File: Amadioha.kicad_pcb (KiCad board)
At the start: 4 copper layers, 74 x 49.9 mm, 66 parts, among them IC1 ACS37800KMACTR-030B3-I2C, J1 691137710002, J2 SW_Debug, J3 691137710002, K1 G6DN-1A-SL_DC5, Q1 BSS138, Q2 BSS138, Q3 BSS138, SW1 PTS815, SW2 PTS815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

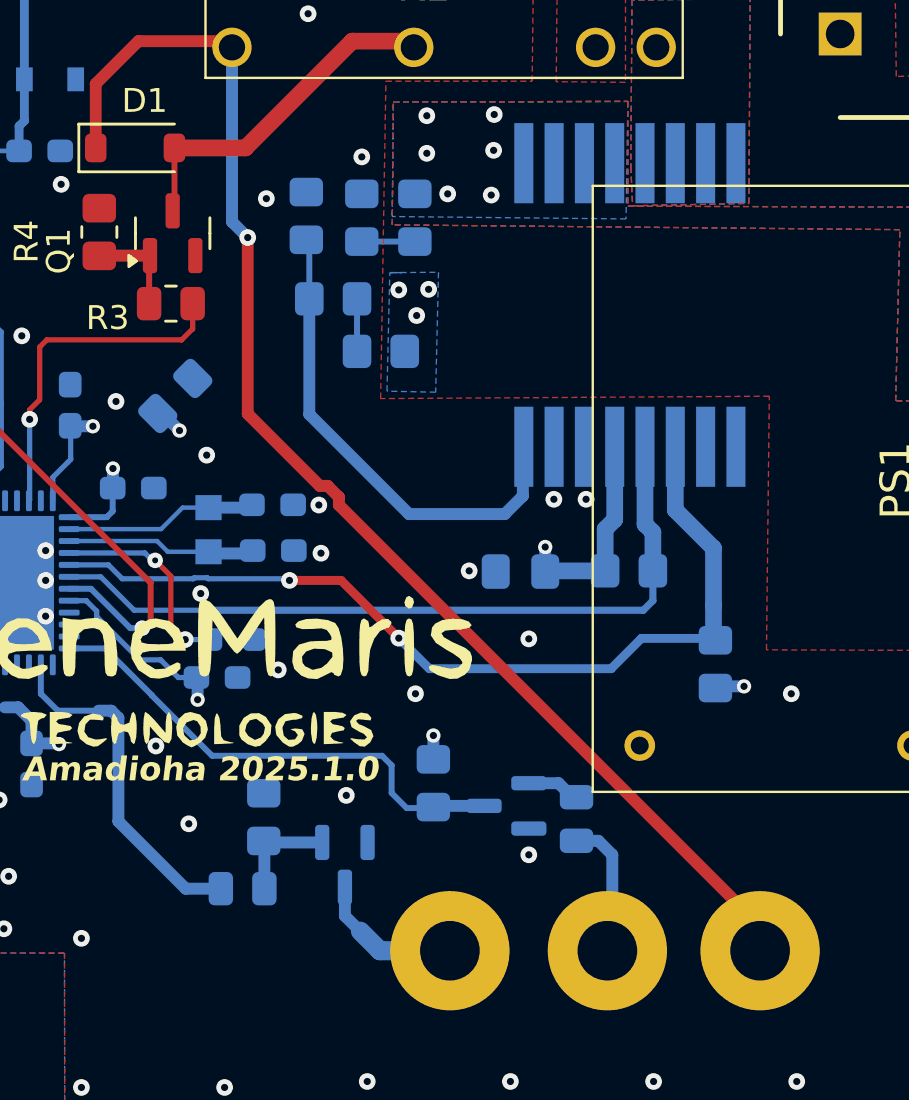
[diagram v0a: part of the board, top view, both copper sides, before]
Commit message: trace width ajdustment
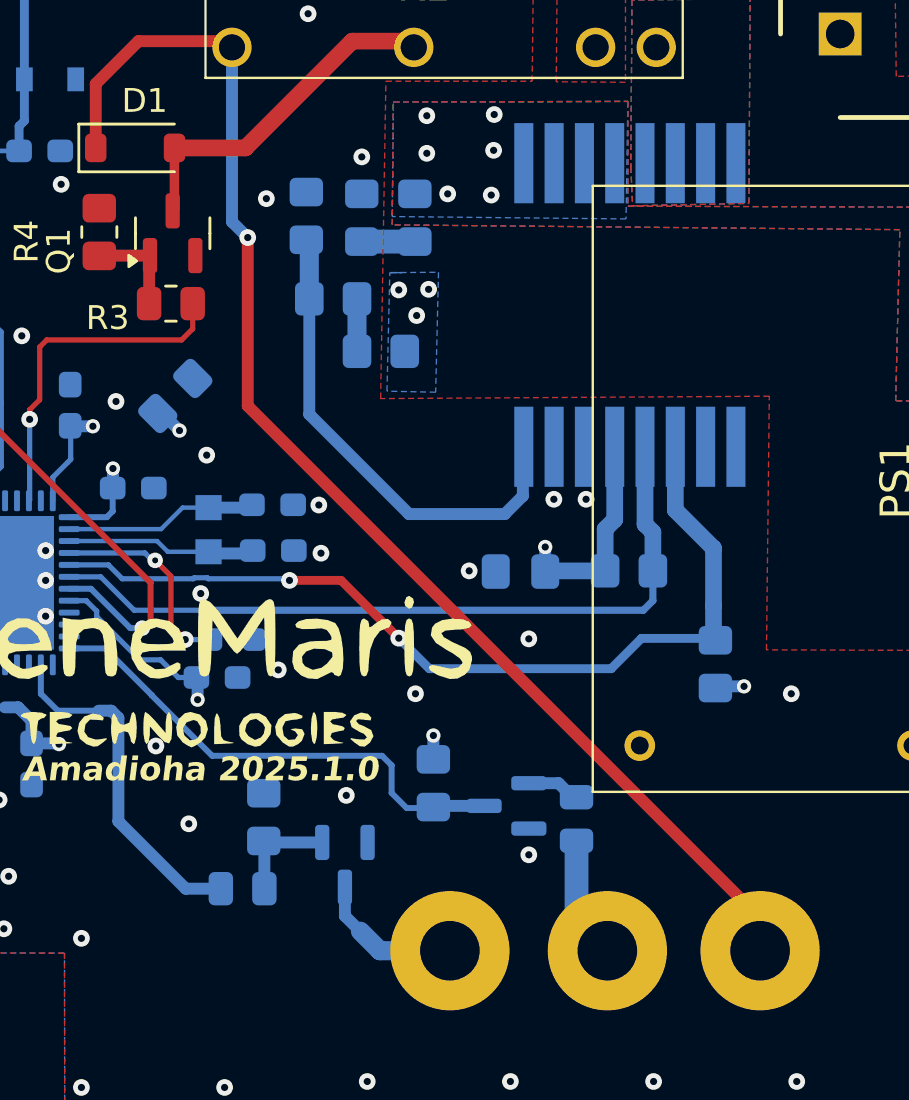
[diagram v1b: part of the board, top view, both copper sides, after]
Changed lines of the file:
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@@
 	)
 	(segment
-		(start 123.6925 101.4925)
-		(end 106.041 83.841)
-		(width 0.5)
-		(layer "F.Cu")
-		(net 11)
-	)
-	(segment
-		(start 106.041 83.841)
-		(end 106.041 83.508214)
-		(width 0.5)
-		(layer "F.Cu")
-		(net 11)
-	)
-	(segment
-		(start 106.041 83.508214)
-		(end 105.571786 83.039)
-		(width 0.5)
-		(layer "F.Cu")
-		(net 11)
-	)
-	(segment
-		(start 102.22 80.02)
-		(end 102.22 72.63)
+		(start 123.6925 102.52)
+		(end 123.6925 101.159714)
 		(width 0.5)
 		(layer "F.Cu")
@@
 	)
 	(segment
-		(start 105.239 83.039)
-		(end 102.22 80.02)
-		(width 0.5)
-		(layer "F.Cu")
-		(net 11)
-	)
-	(segment
 		(start 95.85 66.19)
 		(end 97.64 64.4)
@@
 	)
 	(segment
-		(start 105.571786 83.039)
-		(end 105.239 83.039)
-		(width 0.5)
-		(layer "F.Cu")
-		(net 11)
-	)
-	(segment
 		(start 95.85 68.875)
 		(end 95.85 66.19)
@@
 	)
 	(segment
-		(start 123.6925 102.52)
-		(end 123.6925 101.4925)
+		(start 102.22 79.687214)
+		(end 102.22 72.63)
+		(width 0.5)
+		(layer "F.Cu")
+		(net 11)
+	)
+	(segment
+		(start 123.6925 101.159714)
+		(end 102.22 79.687214)
 		(width 0.5)
 		(layer "F.Cu")
@@
 	)
 	(segment
-		(start 99.15 71.4375)
-		(end 99.15 68.875)
-		(width 0.25)
-		(layer "F.Cu")
-		(net 12)
-	)
-	(segment
 		(start 102.125 68.875)
 		(end 106.6 64.4)
@@
 	)
 	(segment
+		(start 99.15 71.4375)
+		(end 99.15 68.875)
+		(width 0.4)
+		(layer "F.Cu")
+		(net 12)
+	)
+	(segment
 		(start 106.6 64.4)
 		(end 109.18 64.4)
@@
 		(net 12)
 	)
-	(segment
-		(start 99.075 71.5125)
-		(end 99.15 71.4375)
-		(width 0.25)
-		(layer "F.Cu")
-		(net 12)
-	)
 	(via
 		(at 112.525 68.975)
@@
 	)
 	(segment
-		(start 117.5 98.5)
+		(start 116 97.9125)
+		(end 116 101.2275)
+		(width 1)
+		(layer "B.Cu")
+		(net 15)
+	)
+	(segment
+		(start 116 101.2275)
+		(end 117.085 102.3125)
+		(width 0.5)
+		(layer "B.Cu")
+		(net 15)
+	)
+	(segment
+		(start 117.085 102.3125)
 		(end 117.5 102.3125)
-		(width 0.5)
-		(layer "B.Cu")
-		(net 15)
-	)
-	(segment
-		(start 117.5 102.3125)
-		(end 117.2925 102.52)
 		(width 0.5)
 		(layer "B.Cu")
@@
 	)
 	(segment
-		(start 116.9125 97.9125)
-		(end 117.5 98.5)
-		(width 0.5)
-		(layer "B.Cu")
-		(net 15)
-	)
-	(segment
-		(start 116 97.9125)
-		(end 116.9125 97.9125)
+		(start 117.5 102.3125)
+		(end 117.2925 102.52)
 		(width 0.5)
 		(layer "B.Cu")
@@
 		(start 104.8 75.2)
 		(end 104.8 72.85)
-		(width 0.25)
+		(width 0.8)
 		(layer "B.Cu")
 		(net 19)
@@
 		(start 98.0875 75.4)
 		(end 98.0875 73.425)
-		(width 0.25)
+		(width 0.5)
 		(layer "F.Cu")
 		(net 31)
@@
 		(start 107 72.8)
 		(end 109.225 72.8)
-		(width 0.25)
+		(width 1)
 		(layer "B.Cu")
 		(net 39)
@@
 		(start 106.8 77.4)
 		(end 106.8 75.2)
-		(width 0.25)
+		(width 0.8)
 		(layer "B.Cu")
 		(net 40)

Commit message: 1/7/2026
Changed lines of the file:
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@@
 	(generator_version "9.0")
 	(general
-		(thickness 1.5842)
+		(thickness 1.6002)
 		(legacy_teardrops no)
 	)
@@
 			(layer "F.Mask"
 				(type "Top Solder Mask")
-				(thickness 0.01)
+				(thickness 0.02)
 			)
 			(layer "F.Cu"
@@
 			(layer "B.Mask"
 				(type "Bottom Solder Mask")
-				(thickness 0.01)
+				(thickness 0.016)
 			)
 			(layer "B.Paste"
@@
 		(layer "F.Cu")
 		(pts
-			(xy 151.4 109.1375) (xy 152 58.294312)
+			(xy 89.725 95.175) (xy 89.975 95.225)
 		)
-		(height 7.6)
-		(orientation 1)
+		(height 18.375)
+		(orientation 0)
 		(format
 			(prefix "")
@@
 			(keep_text_aligned yes)
 		)
-		(gr_text "50.8432 mm"
-			(at 157.2 83.715906 90)
-			(layer "F.Cu")
-			(effects
-				(font
-					(size 1.5 1.5)
-					(thickness 0.3)
-				)
-			)
-		)
-	)
-	(dimension
-		(type orthogonal)
-		(layer "F.Cu")
-		(pts
-			(xy 122.825 109.9375) (xy 122.825 58.3375)
-		)
-		(height 44)
-		(orientation 1)
-		(format
-			(prefix "")
-			(suffix "")
-			(units 3)
-			(units_format 1)
-			(precision 4)
-		)
-		(style
-			(thickness 0.2)
-			(arrow_length 1.27)
-			(text_position_mode 0)
-			(arrow_direction outward)
-			(extension_height 0.58642)
-			(extension_offset 0.5)
-			(keep_text_aligned yes)
-		)
-		(gr_text "51.6000 mm"
-			(at 165.025 84.1375 90)
+		(gr_text "0.2500 mm"
+			(at 89.85 111.75 0)
 			(layer "F.Cu")
 			(effects
@@
 	)
 	(via
-		(at 89.2 94.6)
+		(at 89.175 94.6)
 		(size 0.7)
 		(drill 0.3)
@@
 	)
 	(segment
-		(start 89.4 70.4)
-		(end 89.4 69.6)
-		(width 0.2)
-		(layer "F.Cu")
-		(net 47)
-	)
-	(segment
-		(start 89.4 75.4)
-		(end 89.4 70.4)
+		(start 89.4 69.6)
+		(end 89.4 75.4)
 		(width 0.2)
 		(layer "F.Cu")
@@
 	)
 	(segment
-		(start 89.4 69.6)
-		(end 89.8 69.2)
+		(start 89.7125 69.2875)
+		(end 89.4 69.6)
 		(width 0.2)
 		(layer "F.Cu")
@@
 	)
 	(segment
-		(start 89.8 75.8)
-		(end 89.4 75.4)
+		(start 89.4 75.4)
+		(end 89.8 75.8)
 		(width 0.2)
 		(layer "F.Cu")
@@
 	)
 	(via
-		(at 89.8 69.2)
+		(at 89.7125 69.2875)
 		(size 0.6)
 		(drill 0.3)
@@
 	)
 	(segment
-		(start 90 69)
-		(end 92.6375 69)
-		(width 0.2)
-		(layer "B.Cu")
-		(net 47)
-	)
-	(segment
 		(start 92.86 67.74)
 		(end 92.86 66)
@@
 	)
 	(segment
-		(start 89.8 69.2)
-		(end 90 69)
-		(width 0.2)
-		(layer "B.Cu")
-		(net 47)
-	)
-	(segment
 		(start 92.6375 67.9625)
 		(end 92.86 67.74)
@@
 		(width 0.2)
 		(layer "B.Cu")
+		(net 47)
+	)
+	(segment
+		(start 89.7125 69.2875)
+		(end 90 69)
+		(width 0.2)
+		(layer "B.Cu")
+		(net 47)
+	)
+	(segment
+		(start 90 69)
+		(end 92.6375 69)
+		(width 0.2)
+		(layer "B.Cu")
